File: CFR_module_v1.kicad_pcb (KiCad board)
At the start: 2 copper layers, 80.9 x 70.9 mm, 71 parts, among them J1 Conn_01x20, J2 Conn_01x20, J3 Conn_01x02, J4 Conn_01x02, J5 Conn_01x02, Q1 NPN

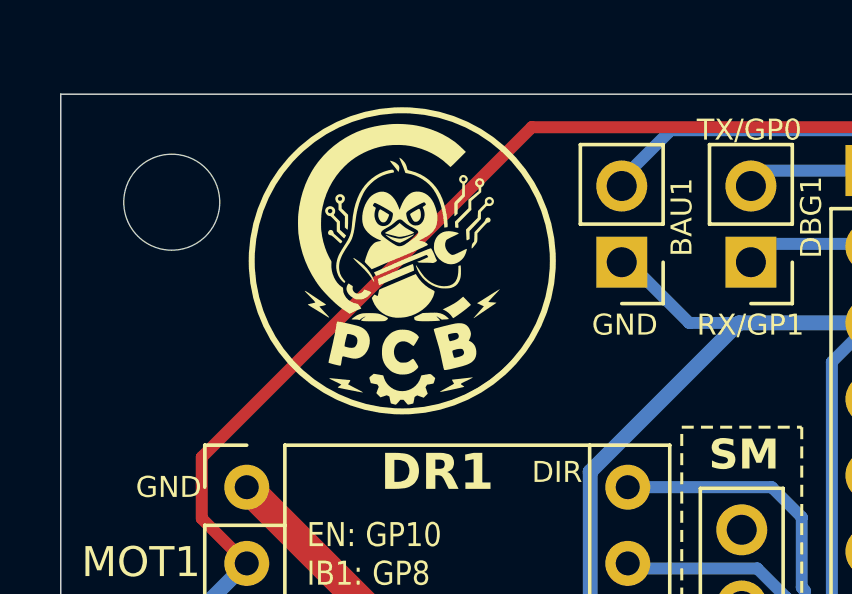
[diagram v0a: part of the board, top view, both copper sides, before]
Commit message: Placement composant front et silkscreen
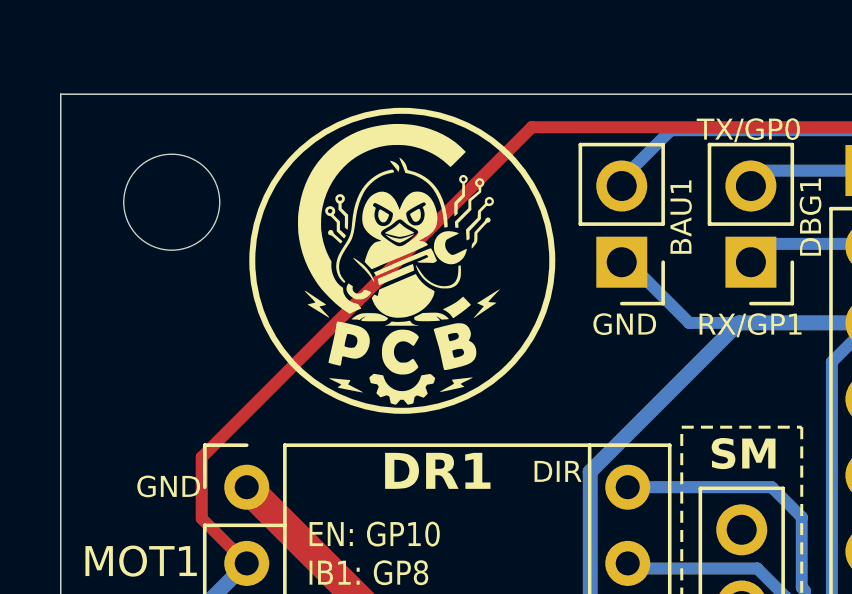
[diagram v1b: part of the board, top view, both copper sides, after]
